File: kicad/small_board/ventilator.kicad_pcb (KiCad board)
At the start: 2 copper layers, 53 parts, among them J1 PJ-202A, J2 Conn_01x02, J3 Conn_01x02, J4 Conn_01x02, J5 Conn_01x02, J6 Conn_01x02, J7 Conn_01x02, J8 Conn_01x02, J9 Conn_01x02, Q1 IRLIZ44NPBF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

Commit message: decent placement for kicad small board
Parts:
- added H1: MountingHole_Pad, MountingHole:MountingHole_2.2mm_M2, F.Cu at (3.00, 3.00)
- added H2: MountingHole_Pad, MountingHole:MountingHole_2.2mm_M2, F.Cu at (87.0, 3.00)
- added H3: MountingHole_Pad, MountingHole:MountingHole_2.2mm_M2, F.Cu at (3.00, 97.0)
- added H4: MountingHole_Pad, MountingHole:MountingHole_2.2mm_M2, F.Cu at (87.0, 97.0)
- moved RV1 245.4 mm to (19.0, 3.00), turned to 90 degrees
- moved J8 240.7 mm to (10.0, 95.0), turned to 0 degrees
- moved C1 239.5 mm to (11.0, 14.0), turned to 180 degrees
- moved D11 238.5 mm to (9.00, 87.0), turned to 0 degrees
- moved J2 235.4 mm to (3.00, 21.0), turned to 180 degrees
- moved R11 235.3 mm to (8.26, 76.8), turned to 0 degrees
- moved Q5 234.4 mm to (10.0, 82.9), turned to 0 degrees
- moved C2 232.4 mm to (20.0, 14.0), turned to 180 degrees
- moved RV2 230.9 mm to (37.0, 3.00), turned to 90 degrees
- moved C5 227.5 mm to (29.0, 14.0), turned to 180 degrees
- moved J3 226.3 mm to (3.00, 11.0), turned to 0 degrees
- moved D9 223.2 mm to (13.3, 67.3), turned to 180 degrees
- moved RV3 219.1 mm to (55.0, 3.00), turned to 90 degrees
- moved R9 219.1 mm to (15.9, 73.0), turned to 180 degrees
- moved J7 215.1 mm to (23.0, 95.0), turned to 0 degrees
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
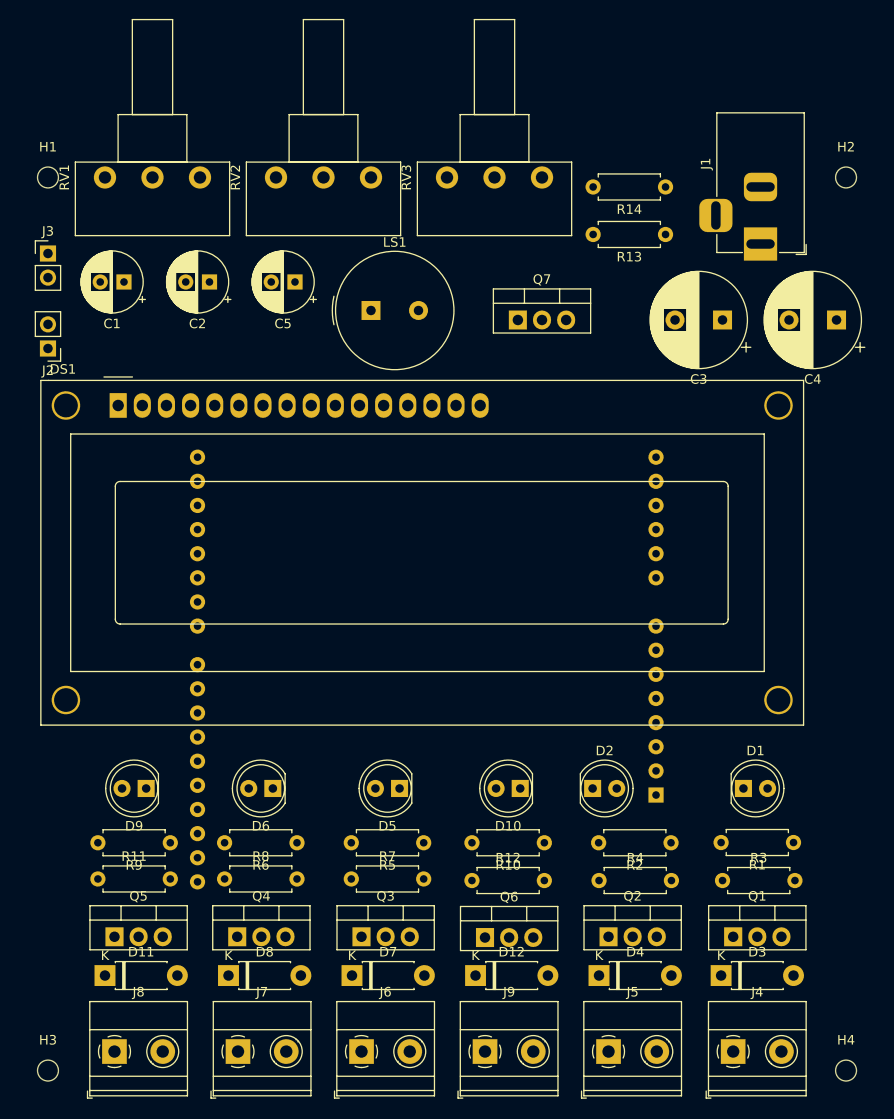
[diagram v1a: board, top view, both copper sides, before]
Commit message: finishes layout of small kicad PCB
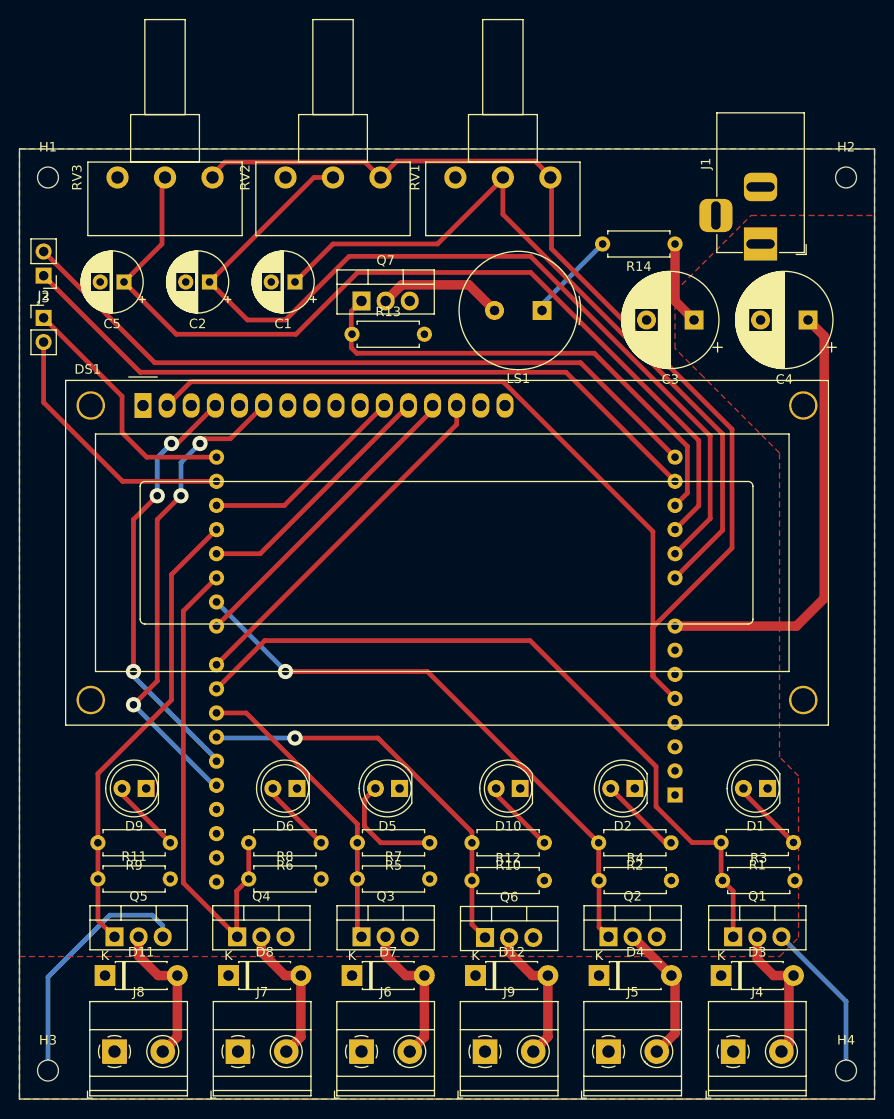
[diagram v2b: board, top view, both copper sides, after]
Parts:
- moved RV1 36.9 mm to (55.9, 3.00)
- moved RV3 34.7 mm to (20.3, 3.00)
- moved R13 34.6 mm to (35.0, 19.5), turned to 0 degrees
- moved C1 18.0 mm to (29.0, 14.0)
- moved C5 18.0 mm to (11.0, 14.0)
- moved LS1 18.0 mm to (55.0, 17.0), turned to 180 degrees
- moved Q7 16.6 mm to (36.0, 16.0)
- moved R14 6.08 mm to (69.0, 10.0)
- moved D2 4.44 mm to (64.8, 67.3), turned to 180 degrees
- moved J2 3.25 mm to (2.54, 17.8), turned to 0 degrees
- moved C3 3.00 mm to (71.0, 18.0)
- moved C4 3.00 mm to (83.0, 18.0)
- moved DS1 2.61 mm to (13.0, 27.0)
- moved D6 2.54 mm to (29.2, 67.3)
- moved R6 2.54 mm to (31.8, 73.0)
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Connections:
- net Net-(D11-Pad2) renamed /Q5_D
- net Net-(D12-Pad2) renamed /Q6_D
- net Net-(D3-Pad2) renamed /Q1_D
- net Net-(D4-Pad2) renamed /Q2_D
- net Net-(D7-Pad2) renamed /Q3_D
- net Net-(D8-Pad2) renamed /Q4_D
- net Net-(LS1-Pad2) renamed /Q7_D
- A1 pad 25: /FILL -> /INS_OPEN
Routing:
- net +5V: track 0.00 -> 179.8 mm
- net /POT_1: track 0.00 -> 96.4 mm
- net /POT_2: track 0.00 -> 95.9 mm
- net /POT_0: track 0.00 -> 80.3 mm
- net /EXP_OPEN: track 0.00 -> 76.9 mm
- net Net-(A1-Pad13): track 0.00 -> 75.4 mm
- net Net-(A1-Pad14): track 0.00 -> 75.4 mm
- net /EXP_CLOSE: track 0.00 -> 61.1 mm, vias 0 -> 1
- net +12V: track 0.00 -> 55.7 mm
- net /INS_CLOSE: track 0.00 -> 52.0 mm
- net /BUZZER: track 0.00 -> 51.8 mm
- net /LCD_EN: track 0.00 -> 50.8 mm, vias 0 -> 3
- net /FILL_CLOSE: track 0.00 -> 48.8 mm
- net /LCD_RS: track 0.00 -> 45.4 mm, vias 0 -> 3
- net GND: track 0.00 -> 43.1 mm
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- added copper zone on F.Cu, net +12V
- added copper zone on B.Cu, net GND
- added copper zone on F.Cu, net GND
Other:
- board outline added: 90 x 100 mm
- net class 12V added: clearance 0.2, trace_width 1, via_dia 1.6, via_drill 0.8
- net class Default: trace_width 0.25 -> 0.5; via_dia 0.8 -> 1.6; via_drill 0.4 -> 0.8

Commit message: touches up small kicad pcb layout
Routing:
- net /Q1_D: track 15.4 -> 17.2 mm

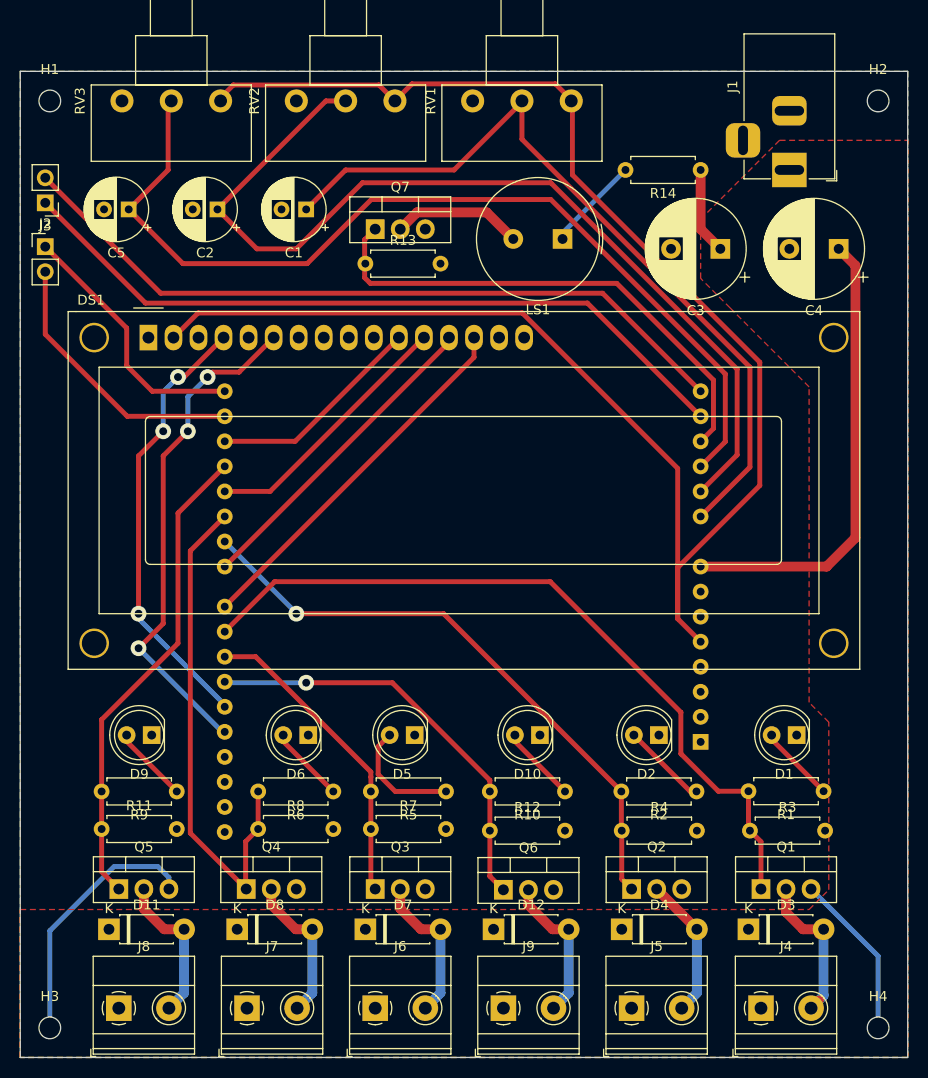
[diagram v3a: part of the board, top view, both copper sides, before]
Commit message: fixes transistor order, adds ground test point
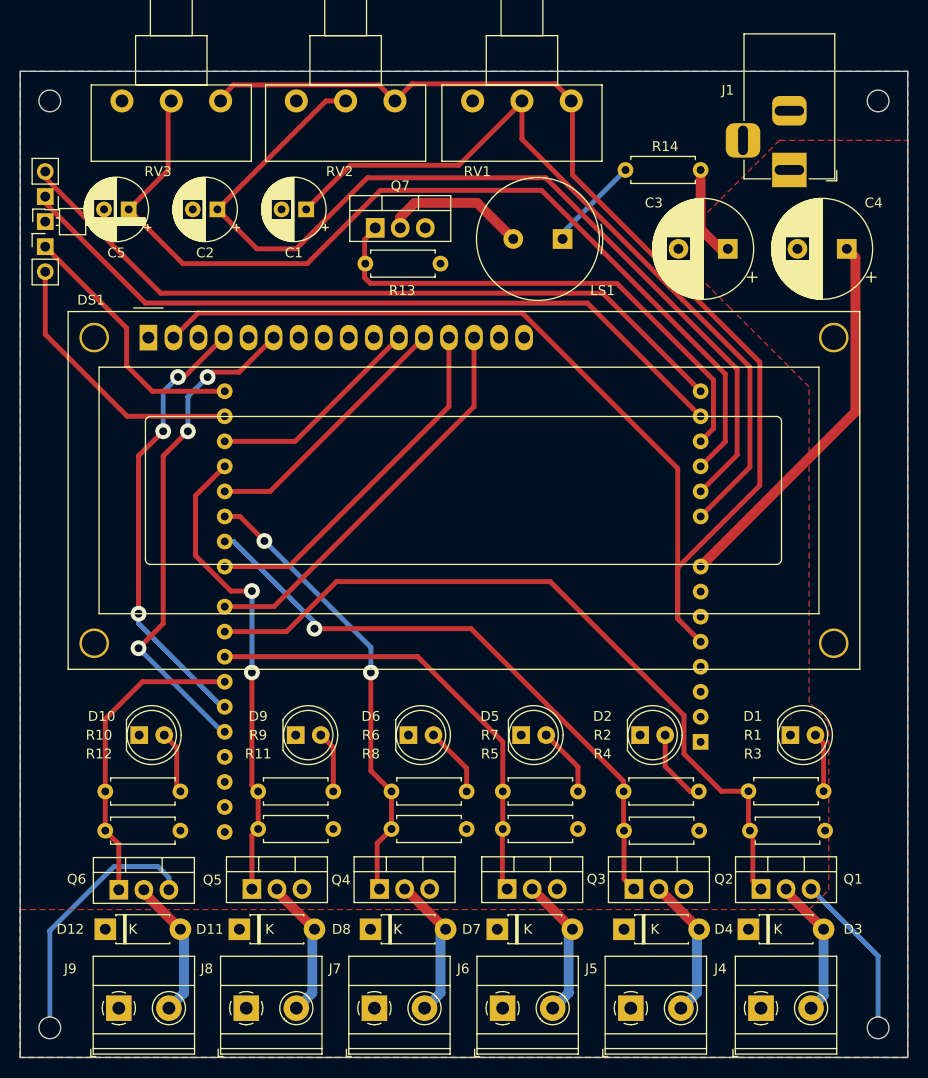
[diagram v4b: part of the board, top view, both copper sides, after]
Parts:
- added TP1: TestPoint, Connector_PinHeader_2.54mm:PinHeader_1x01_P2.54mm_Horizontal, F.Cu at (2.54, 15.2)
- moved D10 40.6 mm to (12.1, 67.3), turned to 0 degrees
- moved D12 39.4 mm to (8.62, 87.0)
- moved J9 39.0 mm to (10.0, 95.0)
- moved Q6 39.0 mm to (10.0, 83.0)
- moved R10 39.0 mm to (16.2, 73.0)
- moved R12 39.0 mm to (8.62, 77.0)
- moved R9 15.9 mm to (31.8, 73.0)
- moved R11 15.9 mm to (24.1, 76.8)
- moved D9 14.6 mm to (27.9, 67.3), turned to 0 degrees
- moved D8 13.5 mm to (35.5, 87.0)
- moved R6 13.5 mm to (45.3, 73.0)
- moved R8 13.5 mm to (37.6, 76.8)
- moved Q4 13.5 mm to (36.4, 82.9)
- moved Q5 13.5 mm to (23.5, 82.9)
- moved D7 13.4 mm to (48.4, 87.0)
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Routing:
- net /INS_OPEN: track 31.7 -> 46.9 mm
- net /FILL_OPEN: track 42.7 -> 31.6 mm, vias 1 -> 0
- net +12V: track 55.7 -> 47.9 mm
- net /INS_CLOSE: track 52.0 -> 46.4 mm, vias 0 -> 2
- net Net-(D5-Pad2): track 12.1 -> 7.05 mm
- net /LCD_DIO6: track 32.6 -> 36.5 mm
- net /Q1_D: track 17.2 -> 14.2 mm
- net /LCD_DIO7: track 37.8 -> 40.7 mm
- net Net-(D1-Pad2): track 7.87 -> 6.03 mm
- net Net-(D9-Pad2): track 7.82 -> 6.24 mm
- net /Q7_D: track 13.3 -> 14.8 mm
- net Net-(D10-Pad2): track 7.82 -> 6.39 mm
- net /Q5_D: track 15.6 -> 14.3 mm
- net /EXP_CLOSE: track 61.1 -> 62.3 mm
- net /Q3_D: track 15.6 -> 14.4 mm
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
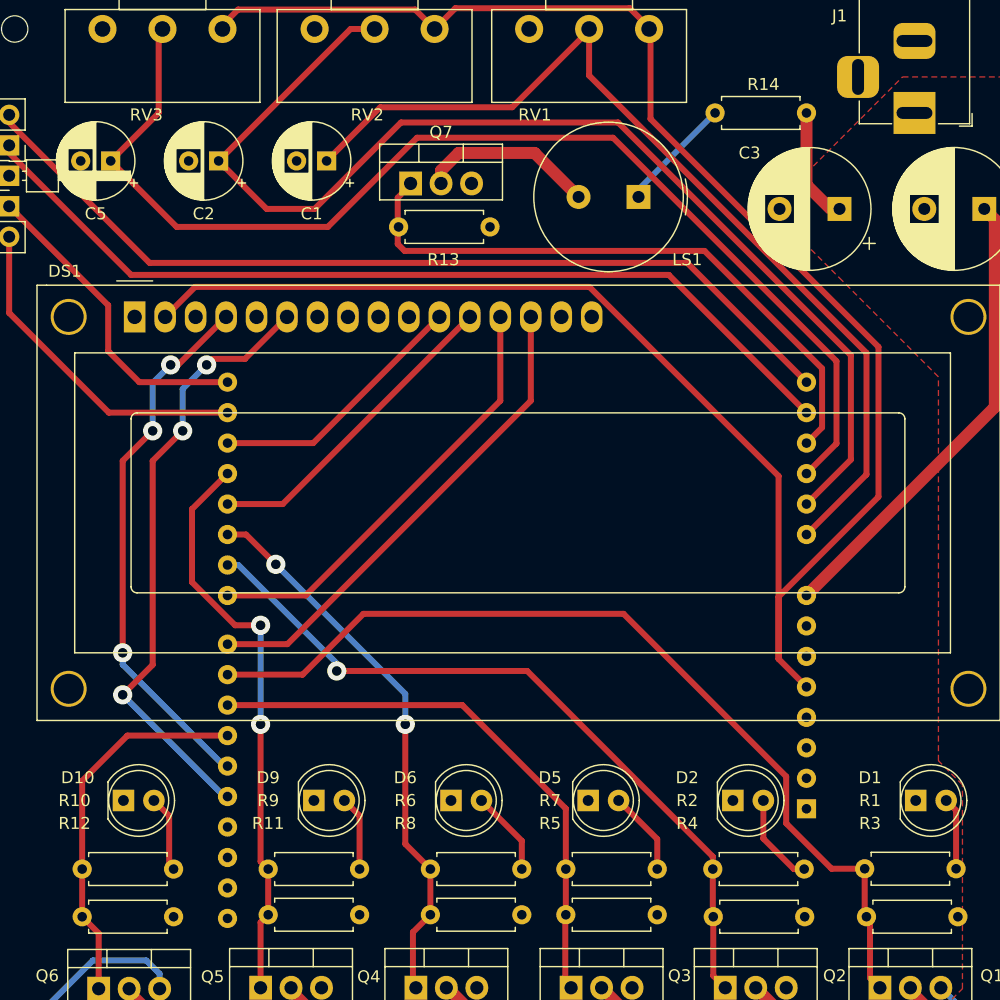
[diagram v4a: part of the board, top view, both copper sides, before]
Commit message: finish silkscreen for small kicad board
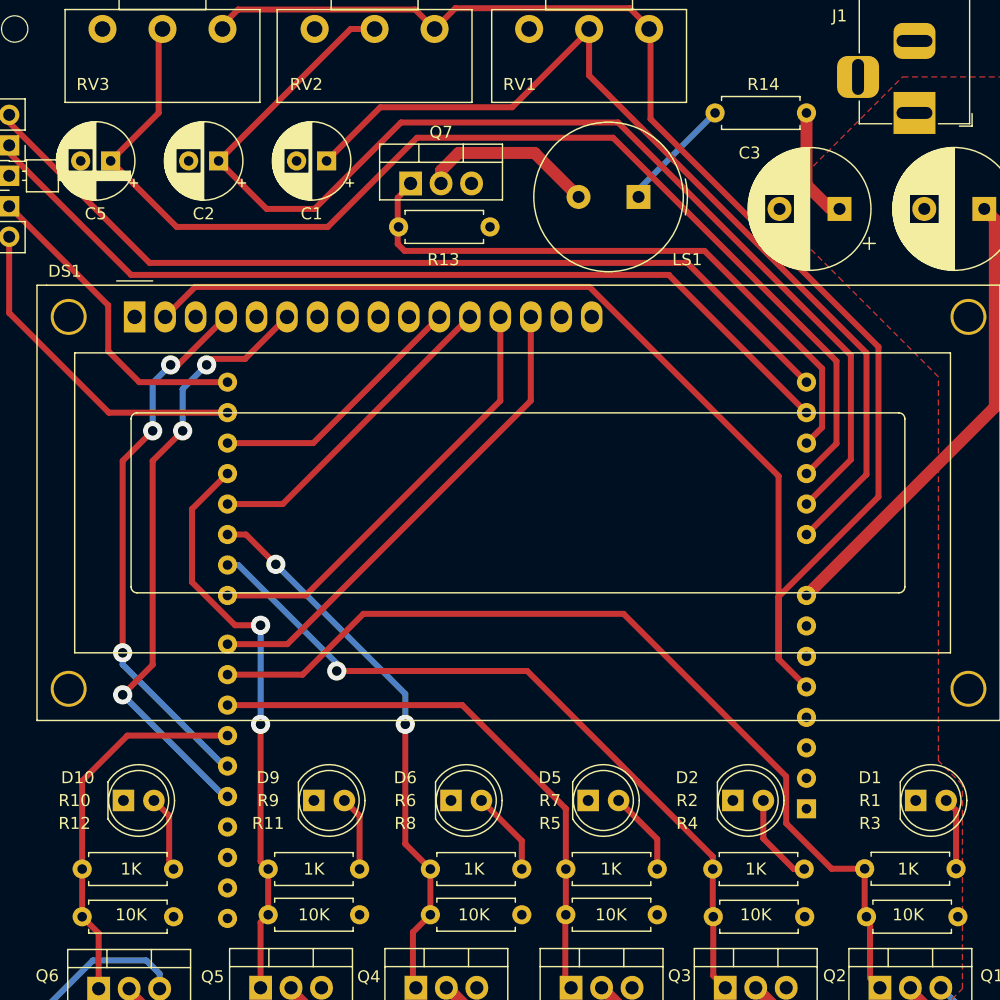
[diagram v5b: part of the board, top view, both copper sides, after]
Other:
- board text added: "10K"
- board text added: "1K"
- board text added: "OUTPUT 1"
- board text added: "OUTPUT 2"
- board text added: "OUTPUT 3"
- board text added: "OUTPUT 4"
- board text added: "OUTPUT 5"
- board text added: "OUTPUT 6"
- board text added: "POT 1"
- board text added: "POT 2"
- board text added: "POT 3"
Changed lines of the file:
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@@
   (general
     (thickness 1.6)
-    (drawings 4)
+    (drawings 25)
     (tracks 210)
     (modules 58)
@@
     (descr "Potentiometer, horizontal, Piher T-16H Single, http://www.piher-nacesa.com/pdf/22-T16v03.pdf")
     (tags "Potentiometer horizontal Piher T-16H Single")
-    (fp_text reference "RV3" (at -7.16 -6.35 180) (layer "F.SilkS")
+    (fp_text reference "RV3" (at -4.62 -10.795 180) (layer "F.SilkS")
       (effects (font (size 1 1) (thickness 0.15)))
     )
@@
     (descr "Potentiometer, horizontal, Piher T-16H Single, http://www.piher-nacesa.com/pdf/22-T16v03.pdf")
     (tags "Potentiometer horizontal Piher T-16H Single")
-    (fp_text reference "RV2" (at -7.16 -5.615 180) (layer "F.SilkS")
+    (fp_text reference "RV2" (at -4.62 -10.695 180) (layer "F.SilkS")
       (effects (font (size 1 1) (thickness 0.15)))
     )
@@
     (descr "Potentiometer, horizontal, Piher T-16H Single, http://www.piher-nacesa.com/pdf/22-T16v03.pdf")
     (tags "Potentiometer horizontal Piher T-16H Single")
-    (fp_text reference "RV1" (at -7.16 -9.525 180) (layer "F.SilkS")
+    (fp_text reference "RV1" (at -4.62 -10.795 180) (layer "F.SilkS")
       (effects (font (size 1 1) (thickness 0.15)))
     )
@@
     (descr "Arduino UNO R3, http://www.mouser.com/pdfdocs/Gravitech_Arduino_Nano3_0.pdf")
     (tags "Arduino UNO R3")
-    (fp_text reference "A1" (at 1.27 3.81 270) (layer "B.SilkS")
+    (fp_text reference "A1" (at 1.27 3.81 270) (layer "B.SilkS") hide
       (effects (font (size 1 1) (thickness 0.15)) (justify mirror))
     )
@@
     )
   )
+  (gr_text "POT 3" (at 15.24 6.35) (layer "B.SilkS")
+    (effects (font (size 1 1) (thickness 0.15)) (justify mirror))
+  )
+  (gr_text "POT 2" (at 33.02 6.35) (layer "B.SilkS")
+    (effects (font (size 1 1) (thickness 0.15)) (justify mirror))
+  )
+  (gr_text "POT 1" (at 50.8 6.35) (layer "B.SilkS")
+    (effects (font (size 1 1) (thickness 0.15)) (justify mirror))
+  )
+  (gr_text "OUTPUT 6" (at 12.7 99.06) (layer "B.SilkS")
+    (effects (font (size 1 1) (thickness 0.15)) (justify mirror))
+  )
+  (gr_text "OUTPUT 5" (at 25.4 99.06) (layer "B.SilkS")
+    (effects (font (size 1 1) (thickness 0.15)) (justify mirror))
+  )
+  (gr_text "OUTPUT 4" (at 38.735 99.06) (layer "B.SilkS")
+    (effects (font (size 1 1) (thickness 0.15)) (justify mirror))
+  )
+  (gr_text "OUTPUT 3" (at 51.435 99.06) (layer "B.SilkS")
+    (effects (font (size 1 1) (thickness 0.15)) (justify mirror))
+  )
+  (gr_text "OUTPUT 2" (at 64.135 99.06) (layer "B.SilkS")
+    (effects (font (size 1 1) (thickness 0.15)) (justify mirror))
+  )
+  (gr_text "OUTPUT 1" (at 78.105 99.06) (layer "B.SilkS")
+    (effects (font (size 1 1) (thickness 0.15)) (justify mirror))
+  )
+  (gr_text "10K" (at 12.7 76.835) (layer "F.SilkS")
+    (effects (font (size 1 1) (thickness 0.15)))
+  )
+  (gr_text "10K" (at 27.94 76.835) (layer "F.SilkS")
+    (effects (font (size 1 1) (thickness 0.15)))
+  )
+  (gr_text "10K" (at 41.275 76.835) (layer "F.SilkS")
+    (effects (font (size 1 1) (thickness 0.15)))
+  )
+  (gr_text "10K" (at 52.705 76.835) (layer "F.SilkS")
+    (effects (font (size 1 1) (thickness 0.15)))
+  )
+  (gr_text "10K" (at 64.77 76.835) (layer "F.SilkS")
+    (effects (font (size 1 1) (thickness 0.15)))
+  )
+  (gr_text "10K" (at 77.47 76.835) (layer "F.SilkS")
+    (effects (font (size 1 1) (thickness 0.15)))
+  )
+  (gr_text "1K" (at 77.47 73.025) (layer "F.SilkS")
+    (effects (font (size 1 1) (thickness 0.15)))
+  )
+  (gr_text "1K" (at 64.77 73.025) (layer "F.SilkS")
+    (effects (font (size 1 1) (thickness 0.15)))
+  )
+  (gr_text "1K" (at 52.705 73.025) (layer "F.SilkS")
+    (effects (font (size 1 1) (thickness 0.15)))
+  )
+  (gr_text "1K" (at 41.275 73.025) (layer "F.SilkS")
+    (effects (font (size 1 1) (thickness 0.15)))
+  )
+  (gr_text "1K" (at 27.94 73.025) (layer "F.SilkS")
+    (effects (font (size 1 1) (thickness 0.15)))
+  )
+  (gr_text "1K" (at 12.7 73.025) (layer "F.SilkS")
+    (effects (font (size 1 1) (thickness 0.15)))
+  )
   (gr_line (start 90 0) (end 0 0) (layer "Edge.Cuts") (width 0.1))

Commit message: clearances
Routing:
- net +5V: track 179.8 -> 190.3 mm
- net /POT_1: track 96.9 -> 103.1 mm
- net /POT_2: track 96.6 -> 102.0 mm
- net Net-(A1-Pad14): track 75.4 -> 79.5 mm
- net Net-(A1-Pad13): track 75.4 -> 79.2 mm
- net /POT_0: track 80.3 -> 83.8 mm
- net /BUZZER: track 51.8 -> 55.0 mm
- net /FILL_CLOSE: track 48.3 -> 50.2 mm
- net /LCD_DIO5: track 26.7 -> 28.3 mm
- net /Q4_D: track 14.5 -> 16.1 mm
- net /Q5_D: track 14.3 -> 15.8 mm
- net /Q3_D: track 14.4 -> 15.9 mm
- net /Q2_D: track 14.4 -> 15.8 mm
- net /Q6_D: track 14.2 -> 15.6 mm
- net /LCD_EN: track 50.8 -> 51.9 mm
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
